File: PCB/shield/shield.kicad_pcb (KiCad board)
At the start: 2 copper layers, 96.3 x 75.4 mm, 13 parts, among them J1 QTR-8A, J10 ESP32_left_m, J11 ESP32_right_m, J12 Barrel_Jack, J2 QMC5883L, J3 Servo, J4 LM2596S_in(+), J5 LM2596S_in(-), J6 LM2596S_out(+), J7 LM2596S_out(-)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

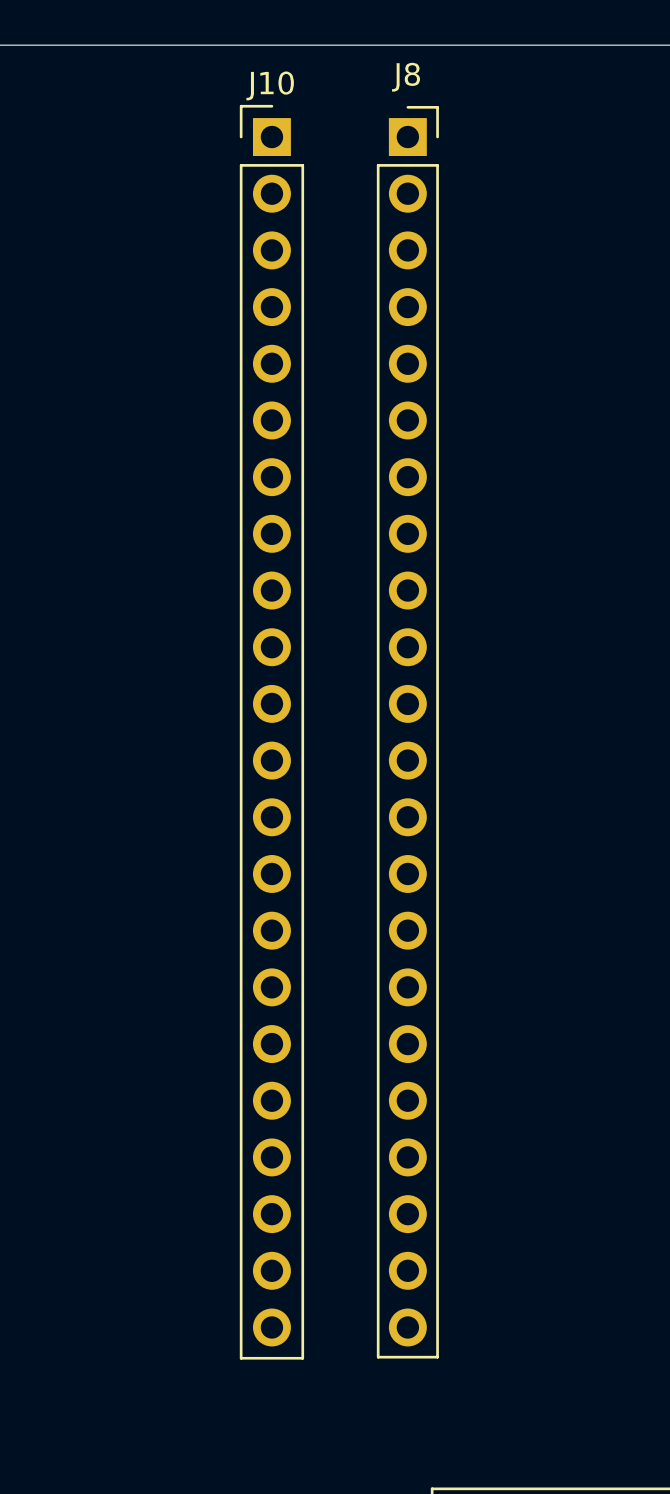
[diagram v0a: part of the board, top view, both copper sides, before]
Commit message: fix: fix length between 2 esp rails
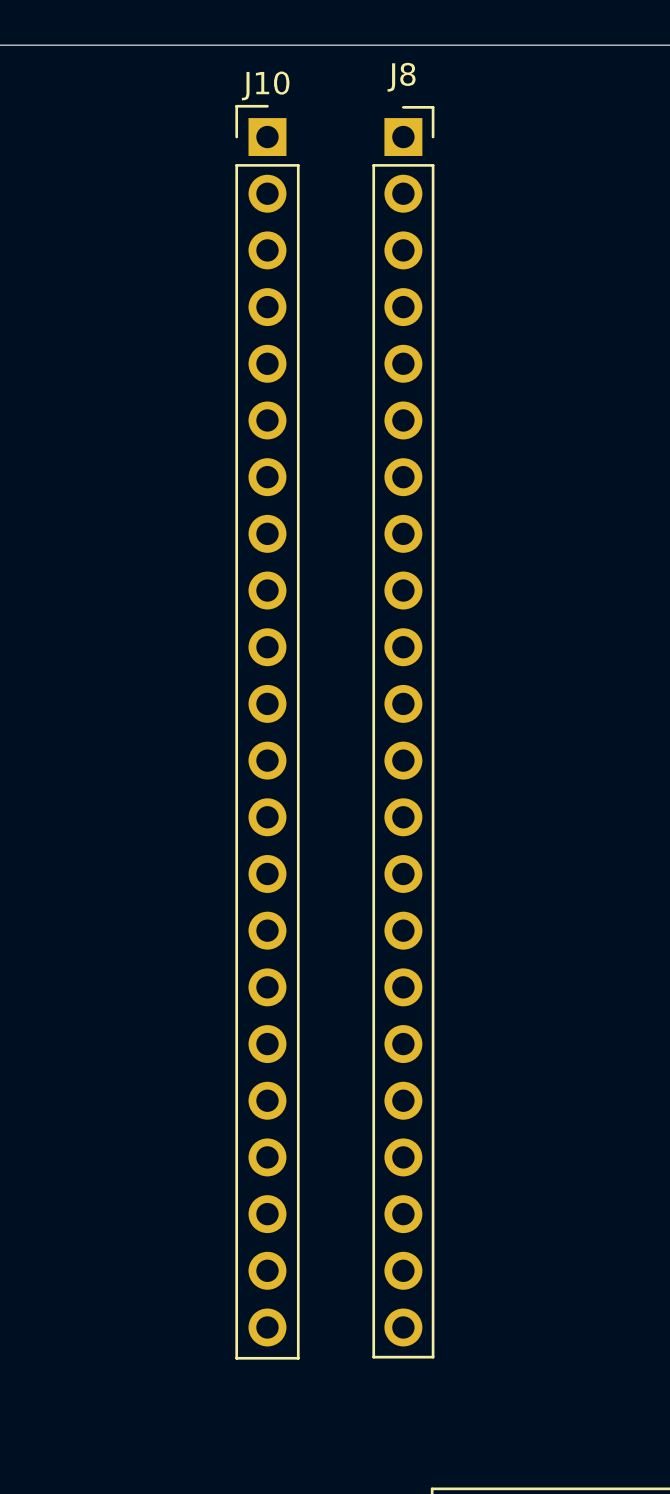
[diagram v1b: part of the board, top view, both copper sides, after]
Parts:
- moved J10 0.20 mm to (112.3, 73.6)
- moved J8 0.20 mm to (118.4, 73.6)
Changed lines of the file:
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@@
 	(footprint "Connector_PinSocket_2.54mm:PinSocket_1x22_P2.54mm_Vertical"
 		(layer "F.Cu")
-		(at 118.5916 73.5838)
+		(at 118.3916 73.5838)
 		(descr "Through hole straight socket strip, 1x22, 2.54mm pitch, single row (from Kicad 4.0.7), script generated")
 		(tags "Through hole socket strip THT 1x22 2.54mm single row")
@@
 	(footprint "Connector_PinHeader_2.54mm:PinHeader_1x22_P2.54mm_Vertical"
 		(layer "F.Cu")
-		(at 112.5016 73.5838)
+		(at 112.3016 73.5838)
 		(descr "Through hole straight pin header, 1x22, 2.54mm pitch, single row")
 		(tags "Through hole pin header THT 1x22 2.54mm single row")
@@
 		(layer "Dwgs.User")
 		(pts
-			(xy 116.7916 71.7838) (xy 146.8916 71.7838)
+			(xy 116.5916 71.7838) (xy 146.8916 71.7838)
 		)
 		(height -10.668)
@@
 			(keep_text_aligned yes)
 		)
-		(gr_text "30.1"
-			(at 131.8416 59.9658 0)
+		(gr_text "30.3"
+			(at 131.7416 59.9658 0)
 			(layer "Dwgs.User")
 			(effects

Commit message: wip: pcb tracks
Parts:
- added J13: Conn_01x06, Connector_JST:JST_XH_B6B-XH-A_1x06_P2.50mm_Vertical, F.Cu at (99.3, 126.1)
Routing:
- net VCC: track 0.00 -> 32.5 mm
- net Net-(J10-Pin_3): track 0.00 -> 6.09 mm
- net Net-(J10-Pin_2): track 0.00 -> 6.09 mm
- net /GPIO4: track 0.00 -> 6.09 mm
- net +3V3: track 0.00 -> 6.09 mm

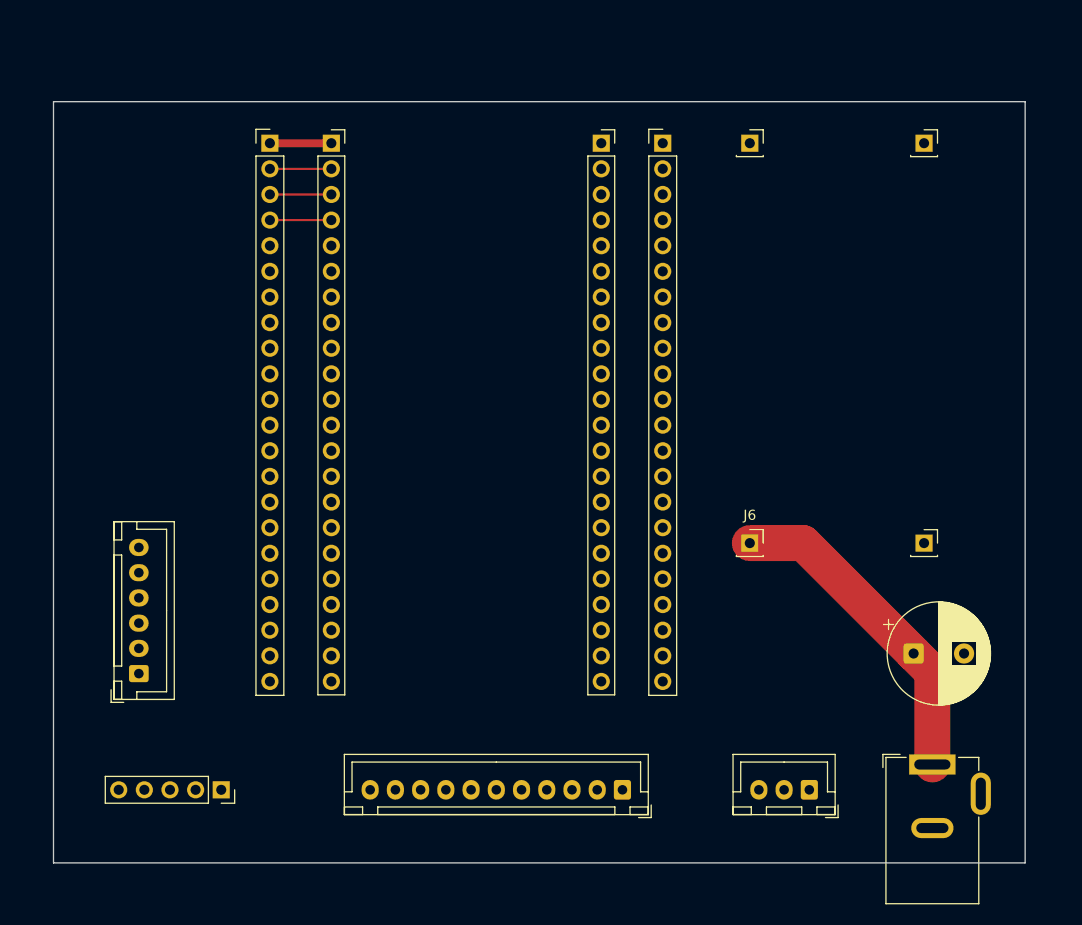
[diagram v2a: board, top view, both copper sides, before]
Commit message: wip: adding tracks on pcb, adding 7805 regulator
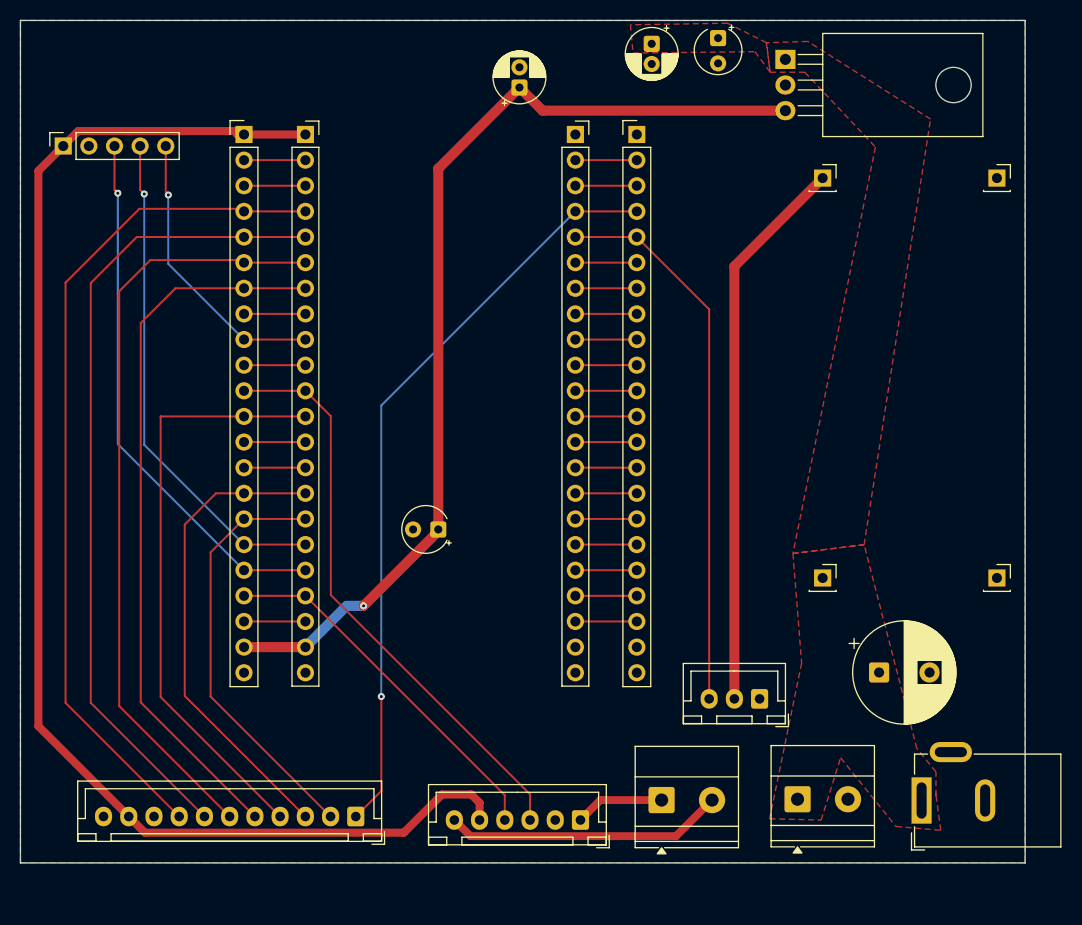
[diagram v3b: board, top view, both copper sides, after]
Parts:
- added C2: 0.22uF, Capacitor_THT:CP_Radial_D5.0mm_P2.00mm, F.Cu at (150.1, 63.7)
- added C3: 0.1uF, Capacitor_THT:CP_Radial_Tantal_D4.5mm_P2.50mm, F.Cu at (156.7, 63.2)
- added C4: 10uF, Capacitor_THT:CP_Radial_D5.0mm_P2.00mm, F.Cu at (137.0, 68.1)
- added C5: 0.1uF, Capacitor_THT:CP_Radial_Tantal_D4.5mm_P2.50mm, F.Cu at (129.0, 111.9)
- added J14: Domino, TerminalBlock_Phoenix:TerminalBlock_Phoenix_MKDS-1,5-2_1x02_P5.00mm_Horizontal, F.Cu at (151.1, 138.7)
- added J15: Domino, TerminalBlock_Phoenix:TerminalBlock_Phoenix_MKDS-1,5-2_1x02_P5.00mm_Horizontal, F.Cu at (164.6, 138.6)
- added U1: L7805, Package_TO_SOT_THT:TO-220-3_Horizontal_TabDown, F.Cu at (163.4, 65.3)
- J4: value LM2596S_in(+) -> LM2596S_out(+)
- J6: value LM2596S_out(+) -> LM2596S_in(+)
- moved J2 65.7 mm to (91.8, 73.9), turned to 90 degrees
- moved J13 46.1 mm to (143.1, 140.7), turned to 180 degrees
- moved J1 26.6 mm to (120.8, 140.3)
- moved J3 10.3 mm to (160.8, 128.7)
- moved J5 8.00 mm to (184.4, 77.0)
- moved J7 8.00 mm to (184.4, 116.7)
- moved J4 8.00 mm to (167.1, 77.0)
- moved J6 8.00 mm to (167.1, 116.7)
- moved C1 3.90 mm to (172.7, 126.0)
- moved J12 3.73 mm to (176.9, 138.7), turned to 90 degrees
- moved J10 2.71 mm to (109.7, 72.7)
- moved J11 2.71 mm to (148.7, 72.7)
- moved J8 2.71 mm to (115.8, 72.7)
- moved J9 2.71 mm to (142.6, 72.7)
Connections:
- net Net-(J3-Pin_2) renamed /V_servo
- J1 pad 1: /GPIO4 -> /GPIO1
- J1 pad 2: /GPIO5 -> /GPIO10
- J1 pad 3: /GPIO6 -> /GPIO9
- J1 pad 4: /GPIO7 -> /GPIO8
- J1 pad 5: /GPIO8 -> /GPIO7
- J1 pad 6: /GPIO9 -> /GPIO6
- J1 pad 7: /GPIO10 -> /GPIO5
- J1 pad 8: /GPIO1 -> /GPIO4
- J13 pad 1: /GPIO17 -> /M1
- J13 pad 3: /GPIO13 -> /GPIO18
- J13 pad 4: /GPIO14 -> /GPIO13
- J13 pad 6: /GPIO18 -> /M2
- J3 pad 1: /GPIO15 -> GND
- J3 pad 3: GND -> /GPIO2
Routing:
- net +3V3: track 6.09 -> 135.7 mm
- net +5V: track 0.00 -> 98.5 mm, vias 0 -> 1
- net /GPIO5: track 0.00 -> 80.7 mm
- net /GPIO4: track 6.09 -> 84.5 mm
- net /GPIO6: track 0.00 -> 76.4 mm
- net /GPIO1: track 0.00 -> 75.1 mm, vias 0 -> 1
- net /GPIO7: track 0.00 -> 71.3 mm
- net /GPIO8: track 0.00 -> 58.9 mm
- net /GPIO18: track 0.00 -> 58.8 mm
- net /V_servo: track 0.00 -> 55.2 mm
- net /GPIO2: track 0.00 -> 54.8 mm
- net /GPIO12+SCL: track 0.00 -> 53.4 mm, vias 0 -> 1
- net /GPIO11+SDA: track 0.00 -> 49.9 mm, vias 0 -> 1
- net /GPIO9: track 0.00 -> 47.1 mm
- net /GPIO10: track 0.00 -> 41.9 mm
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- added copper zone on B.Cu, net GND
- added copper zone on F.Cu, net VCC
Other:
- board size 96.3 x 75.4 mm -> 99.6 x 83.5 mm

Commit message: feat: added pcb traces and remove lm2596s
Added all required pcb traces.
Remove LM2596S footprint
Added LM7805 5V regulator
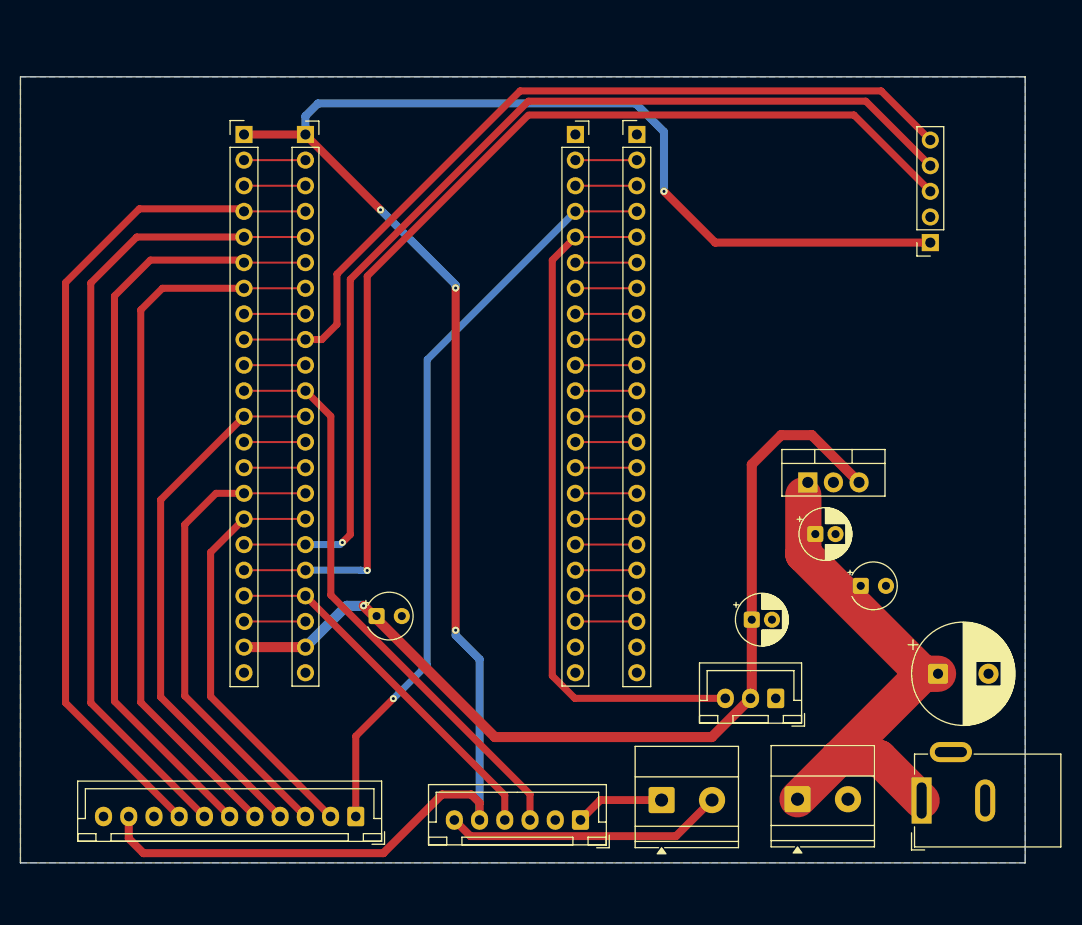
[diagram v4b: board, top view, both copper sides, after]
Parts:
- removed J4: LM2596S_out(+), Connector_PinSocket_2.54mm:PinSocket_1x01_P2.54mm_Vertical
- removed J5: LM2596S_in(-), Connector_PinSocket_2.54mm:PinSocket_1x01_P2.54mm_Vertical
- removed J6: LM2596S_in(+), Connector_PinSocket_2.54mm:PinSocket_1x01_P2.54mm_Vertical
- removed J7: LM2596S_out(-), Connector_PinSocket_2.54mm:PinSocket_1x01_P2.54mm_Vertical
- U1: footprint Package_TO_SOT_THT:TO-220-3_Horizontal_TabDown -> Package_TO_SOT_THT:TO-220-3_Vertical
- moved J2 86.5 mm to (177.7, 83.4), turned to 180 degrees
- moved C4 57.5 mm to (160.1, 120.8), turned to 0 degrees
- moved C3 56.1 mm to (170.9, 117.4), turned to 0 degrees
- moved C2 51.2 mm to (166.4, 112.3), turned to 0 degrees
- moved U1 42.0 mm to (165.6, 107.2), turned to 0 degrees
- moved C5 10.5 mm to (122.9, 120.4), turned to 0 degrees
- moved C1 5.84 mm to (178.5, 126.2)
- moved J3 1.60 mm to (162.4, 128.6)
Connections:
- J3 pad 2: /V_servo -> +5V
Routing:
- net +3V3: track 135.7 -> 196.6 mm, vias 0 -> 4
- net /V_servo: track 55.2 -> 0.00 mm
- net /GPIO16: track 28.5 -> 83.2 mm, vias 1 -> 0
- net /GPIO11+SDA: track 49.9 -> 103.7 mm
- net /GPIO12+SCL: track 53.4 -> 106.9 mm
- net VCC: track 0.00 -> 51.6 mm
- net /GPIO2: track 54.8 -> 68.6 mm
- net /GPIO8: track 58.9 -> 54.1 mm
- net +5V: track 98.5 -> 95.9 mm
- net /GPIO18: track 58.8 -> 57.8 mm
- net /GPIO7: track 71.3 -> 72.1 mm
- removed copper zone on F.Cu, net VCC
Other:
- board size 99.6 x 83.5 mm -> 99.6 x 77.9 mm

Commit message: feat: added silkscreen labels
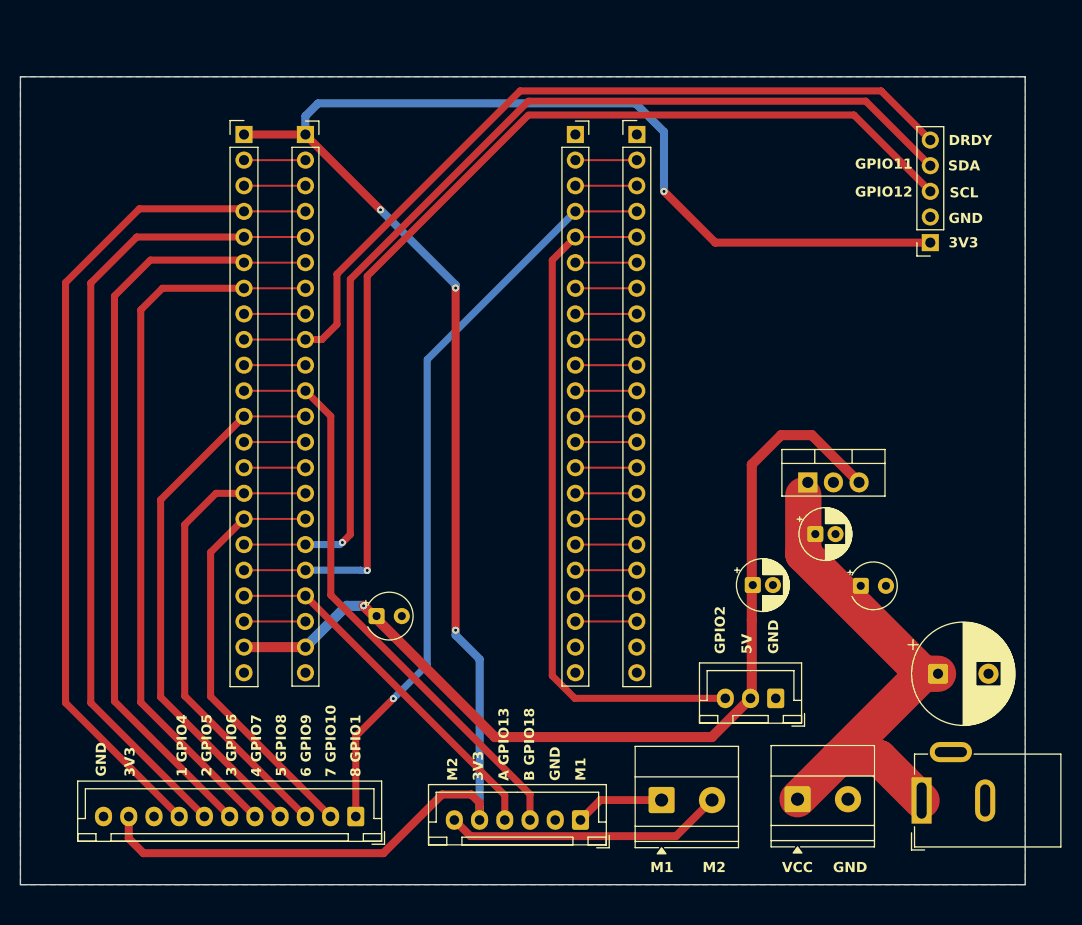
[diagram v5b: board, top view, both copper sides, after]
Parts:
- moved C4 3.43 mm to (160.2, 117.4)
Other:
- board size 99.6 x 77.9 mm -> 99.6 x 80.1 mm
- board text added: "1 GPIO4"
- board text added: "2 GPIO5"
- board text added: "3 GPIO6"
- board text added: "3V3"
- board text added: "4 GPIO7"
- board text added: "5 GPIO8"
- board text added: "5V"
- board text added: "6 GPIO9"
- board text added: "7 GPIO10"
- board text added: "8 GPIO1"
- board text added: "A GPIO13"
- board text added: "B GPIO18"
- board text added: "DRDY"
- board text added: "GND"
- board text added: "GPIO11"
- board text added: "GPIO12"
- board text added: "GPIO2"
- board text added: "M1"
- board text added: "M2"
- board text added: "SCL"
- board text added: "SDA"
- board text added: "VCC"

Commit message: feat: added a  button
Updated button switch THT library
Added a button connected to GPIO15
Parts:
- added SW1: SW_Push, Button_Switch_THT:SW_PUSH_6mm_H5mm, F.Cu at (97.9, 72.7)
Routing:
- net /GPIO15: track 6.09 -> 21.6 mm
- net +3V3: track 196.6 -> 201.9 mm
